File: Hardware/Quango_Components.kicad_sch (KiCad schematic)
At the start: 119 parts, among them J1 Conn_01x12_Male, J2 Conn_01x16_Male, J3 Conn_01x12_Male, J4 Conn_01x12_Male, J5 SWD_Header, J6 Eurorack_10_pin_power, Q1 MMBT3904, U1 LM1117-3.3, U2 STM32G473V, U3 LM1117-5.0, U4 PS508, U5 MCP6002, U6 AS3364, U7 AS3364, U8 AD5676, U9 MCP48CMB21, Y1 8MHz 20pF

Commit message: Updating Controls and Panel to support gates
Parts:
- TP1, TP2, TP3, TP4, TP5, TP6, TP7: footprint Connector_PinSocket_2.54mm:PinSocket_1x01_P2.54mm_Vertical -> Custom_Footprints:1mm_Test_Point
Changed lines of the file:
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@@
       (effects (font (size 1.27 1.27)) (justify left))
     )
-    (property "Footprint" "Connector_PinSocket_2.54mm:PinSocket_1x01_P2.54mm_Vertical" (id 2) (at 162.56 219.71 0)
+    (property "Footprint" "Custom_Footprints:1mm_Test_Point" (id 2) (at 162.56 219.71 0)
       (effects (font (size 1.27 1.27)) hide)
     )
@@
       (effects (font (size 1.27 1.27)) (justify left))
     )
-    (property "Footprint" "Connector_PinSocket_2.54mm:PinSocket_1x01_P2.54mm_Vertical" (id 2) (at 162.56 212.09 0)
+    (property "Footprint" "Custom_Footprints:1mm_Test_Point" (id 2) (at 162.56 212.09 0)
       (effects (font (size 1.27 1.27)) hide)
     )
@@
       (effects (font (size 1.27 1.27)) (justify left))
     )
-    (property "Footprint" "Connector_PinSocket_2.54mm:PinSocket_1x01_P2.54mm_Vertical" (id 2) (at 162.56 209.55 0)
+    (property "Footprint" "Custom_Footprints:1mm_Test_Point" (id 2) (at 162.56 209.55 0)
       (effects (font (size 1.27 1.27)) hide)
     )
@@
       (effects (font (size 1.27 1.27)) (justify left))
     )
-    (property "Footprint" "Connector_PinSocket_2.54mm:PinSocket_1x01_P2.54mm_Vertical" (id 2) (at 162.56 217.17 0)
+    (property "Footprint" "Custom_Footprints:1mm_Test_Point" (id 2) (at 162.56 217.17 0)
       (effects (font (size 1.27 1.27)) hide)
     )
@@
       (effects (font (size 1.27 1.27)) (justify left))
     )
-    (property "Footprint" "Connector_PinSocket_2.54mm:PinSocket_1x01_P2.54mm_Vertical" (id 2) (at 162.56 222.25 0)
+    (property "Footprint" "Custom_Footprints:1mm_Test_Point" (id 2) (at 162.56 222.25 0)
       (effects (font (size 1.27 1.27)) hide)
     )
@@
       (effects (font (size 1.27 1.27)) (justify left))
     )
-    (property "Footprint" "Connector_PinSocket_2.54mm:PinSocket_1x01_P2.54mm_Vertical" (id 2) (at 162.56 214.63 0)
+    (property "Footprint" "Custom_Footprints:1mm_Test_Point" (id 2) (at 162.56 214.63 0)
       (effects (font (size 1.27 1.27)) hide)
     )
@@
       (effects (font (size 1.27 1.27)) (justify left))
     )
-    (property "Footprint" "Connector_PinSocket_2.54mm:PinSocket_1x01_P2.54mm_Vertical" (id 2) (at 162.56 224.79 0)
+    (property "Footprint" "Custom_Footprints:1mm_Test_Point" (id 2) (at 162.56 224.79 0)
       (effects (font (size 1.27 1.27)) hide)
     )
@@
     )
     (path "/32966008-080b-4b6d-b18a-76f78de3a39e"
-      (reference "TP1") (unit 1) (value "TestPoint") (footprint "Connector_PinSocket_2.54mm:PinSocket_1x01_P2.54mm_Vertical")
+      (reference "TP1") (unit 1) (value "TestPoint") (footprint "Custom_Footprints:1mm_Test_Point")
     )
     (path "/1bb5aef1-3a84-4055-bd69-b71df7e9fe50"
-      (reference "TP2") (unit 1) (value "TestPoint") (footprint "Connector_PinSocket_2.54mm:PinSocket_1x01_P2.54mm_Vertical")
+      (reference "TP2") (unit 1) (value "TestPoint") (footprint "Custom_Footprints:1mm_Test_Point")
     )
     (path "/928f3dda-d8e1-4487-a28c-8e719cefdb68"
-      (reference "TP3") (unit 1) (value "TestPoint") (footprint "Connector_PinSocket_2.54mm:PinSocket_1x01_P2.54mm_Vertical")
+      (reference "TP3") (unit 1) (value "TestPoint") (footprint "Custom_Footprints:1mm_Test_Point")
     )
     (path "/6f6acf22-09a4-4af0-8e4d-6e865dd277be"
-      (reference "TP4") (unit 1) (value "TestPoint") (footprint "Connector_PinSocket_2.54mm:PinSocket_1x01_P2.54mm_Vertical")
+      (reference "TP4") (unit 1) (value "TestPoint") (footprint "Custom_Footprints:1mm_Test_Point")
     )
     (path "/16ff65ff-c006-4b1a-a759-716e0e7dcda1"
-      (reference "TP5") (unit 1) (value "TestPoint") (footprint "Connector_PinSocket_2.54mm:PinSocket_1x01_P2.54mm_Vertical")
+      (reference "TP5") (unit 1) (value "TestPoint") (footprint "Custom_Footprints:1mm_Test_Point")
     )
     (path "/7cf45d43-413c-4403-aff1-03fbec52f32a"
-      (reference "TP6") (unit 1) (value "TestPoint") (footprint "Connector_PinSocket_2.54mm:PinSocket_1x01_P2.54mm_Vertical")
+      (reference "TP6") (unit 1) (value "TestPoint") (footprint "Custom_Footprints:1mm_Test_Point")
     )
     (path "/f95c6866-61fc-4e70-b207-d89b04819eae"
-      (reference "TP7") (unit 1) (value "TestPoint") (footprint "Connector_PinSocket_2.54mm:PinSocket_1x01_P2.54mm_Vertical")
+      (reference "TP7") (unit 1) (value "TestPoint") (footprint "Custom_Footprints:1mm_Test_Point")
     )
     (path "/1d12cd53-304c-4f2c-87a4-a7ea0859c7b3"

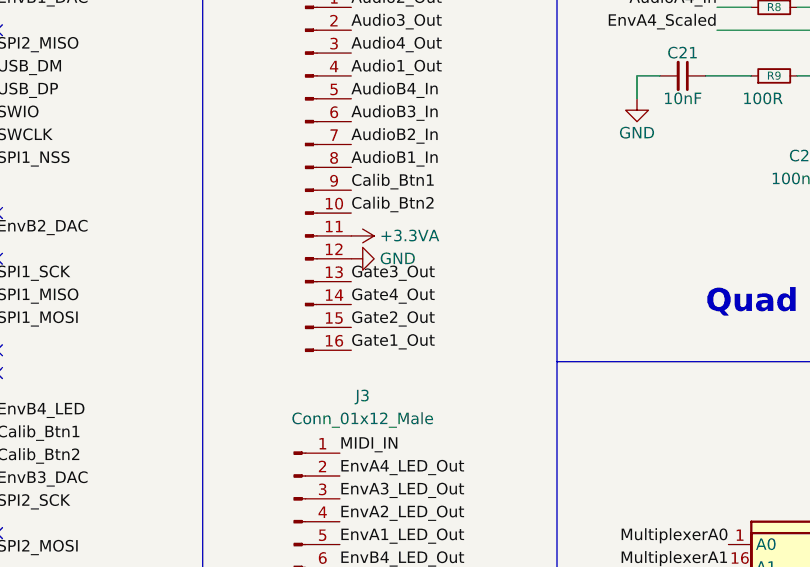
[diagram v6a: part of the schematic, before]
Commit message: Added breakout for gates on component board
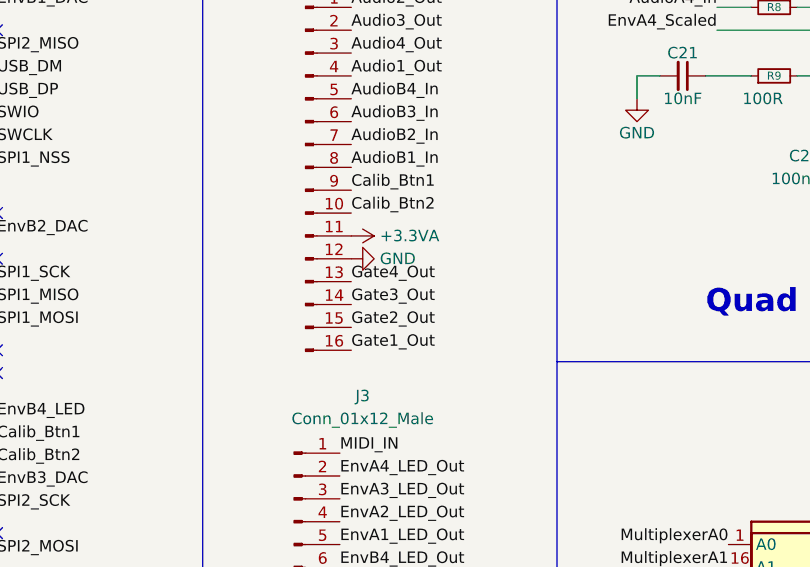
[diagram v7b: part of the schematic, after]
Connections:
- net Gate3_Out: now also J2.14 (Pin_14); no longer J2.13 (Pin_13)
- net Gate4_Out: now also J2.13 (Pin_13); no longer J2.14 (Pin_14)
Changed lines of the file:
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@@
     (effects (font (size 1.27 1.27)) (justify right bottom))
   )
-  (label "Gate4_Out" (at 138.43 96.52 0)
+  (label "Gate4_Out" (at 138.43 93.98 0)
     (effects (font (size 1.27 1.27)) (justify left bottom))
   )
@@
     (effects (font (size 1.27 1.27)) (justify left bottom))
   )
-  (label "Gate3_Out" (at 138.43 93.98 0)
+  (label "Gate3_Out" (at 138.43 96.52 0)
     (effects (font (size 1.27 1.27)) (justify left bottom))
   )
@@
       (reference "J7") (unit 1) (value "Audio_Breakout") (footprint "Connector_PinHeader_2.54mm:PinHeader_2x04_P2.54mm_Vertical")
     )
+    (path "/6505d480-2c4a-43b6-864d-d09e21056980/3b38388f-acb0-409f-a93f-143c9d8182e4"
+      (reference "J8") (unit 1) (value "Gate_Breakout") (footprint "Connector_PinHeader_2.54mm:PinHeader_1x04_P2.54mm_Vertical")
+    )
     (path "/9cc3873a-349e-4fee-be4e-7429042177a8"

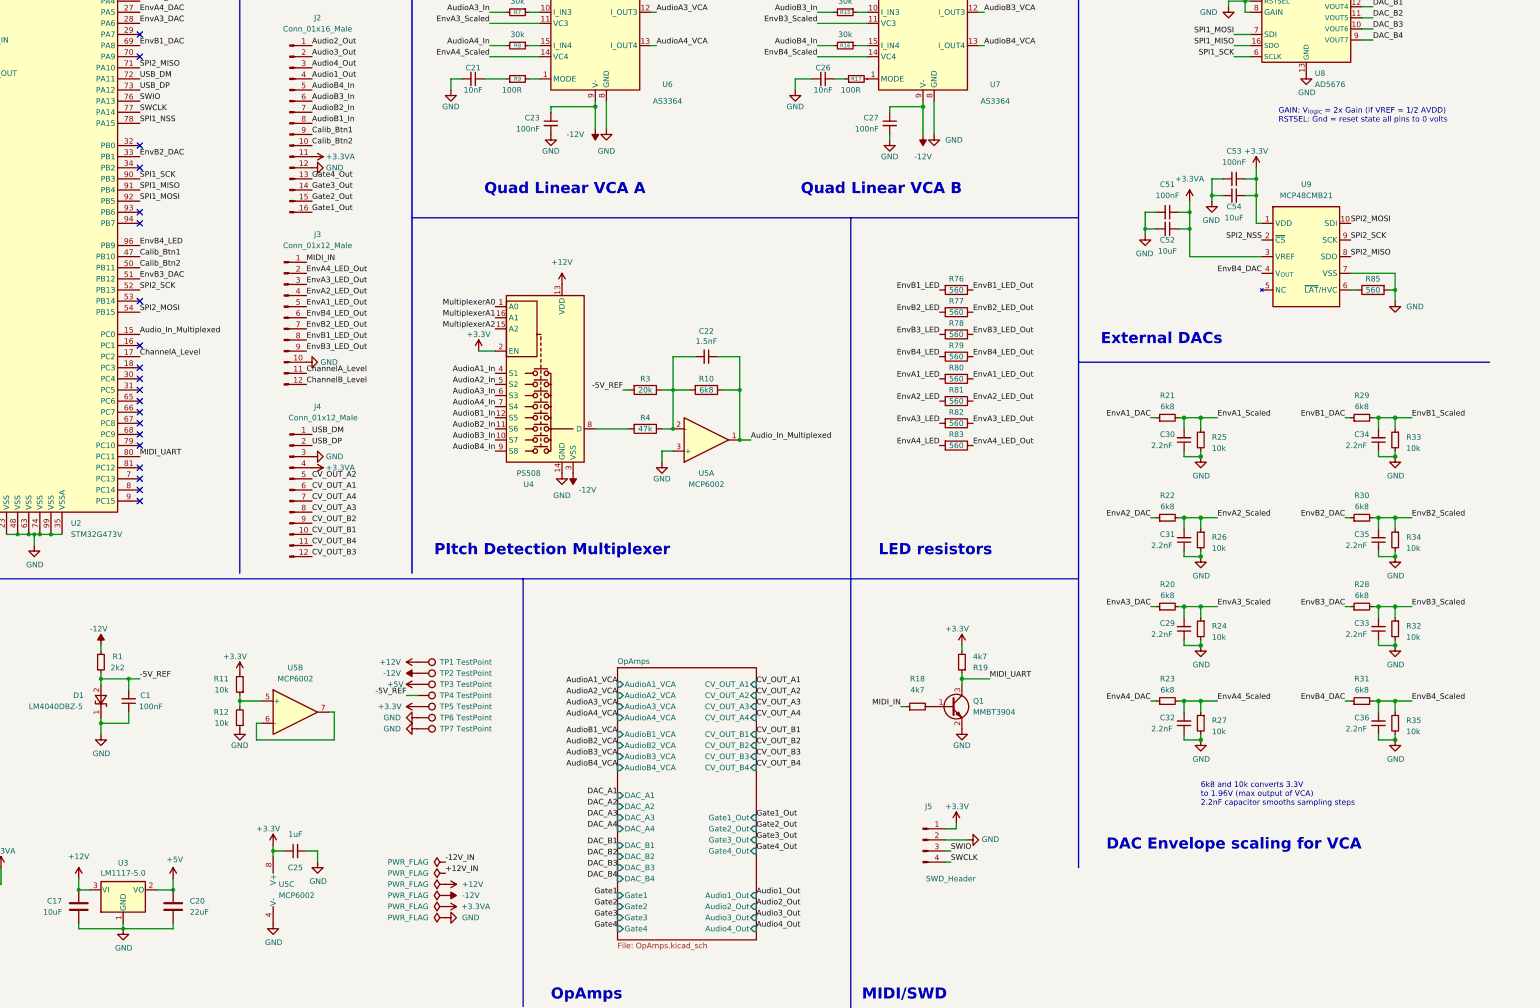
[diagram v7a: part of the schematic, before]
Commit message: Fixed OpAmp Power supply; component board annotations
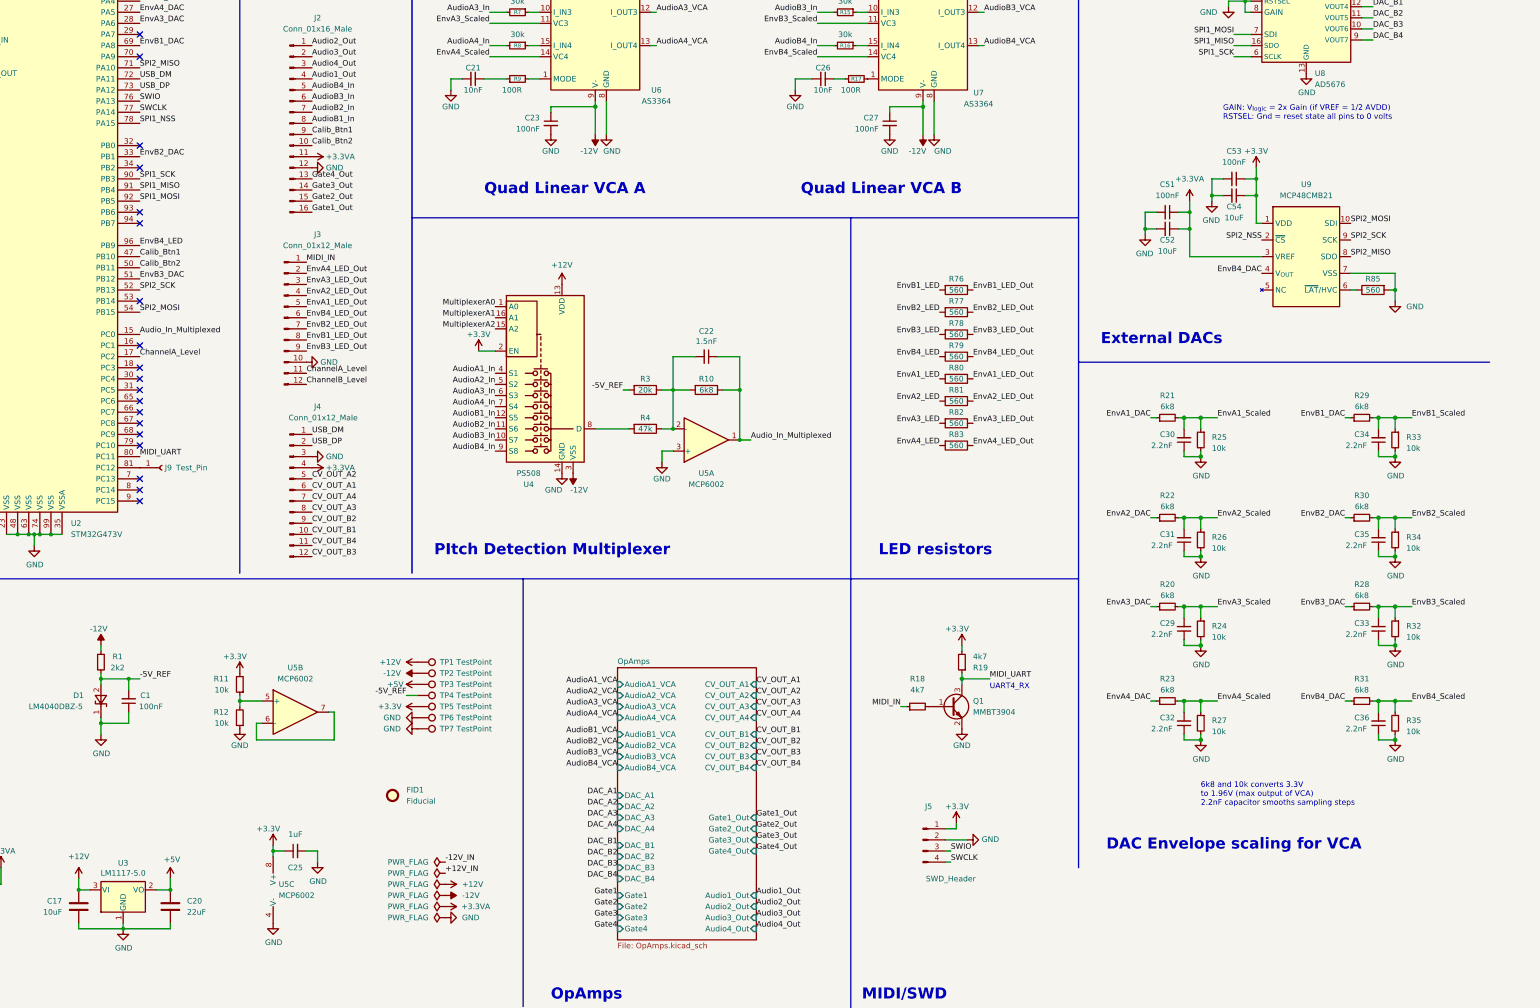
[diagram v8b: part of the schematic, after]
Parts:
- added FID1: Fiducial, Custom_Footprints:4_Layer_Markers, symbol Mechanical:Fiducial
- added J9: Test_Pin, Custom_Footprints:1mm_Test_Point, symbol Connector:Conn_01x01_Female
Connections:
- net at U2.81 (PC12): now also J9.1 (Pin_1)
- no-connect marks 34 -> 33
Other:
- note added: "UART4_RX"
- moved on the sheet: C20
